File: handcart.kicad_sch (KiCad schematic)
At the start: 51 parts, among them J1 ROTARY ENCODER, J10 SPARE_SUPPLY, J12 SPARE_CHARGER, J13 SPARE_BMS, J14 ADD_FAN, J15 EXT_SCREEN, J16 CHARGER, J17 BMS, J2 ARROW_KEYS_1, J3 ARROW_KEYS_2, J4 ARROW_KEYS_3, J5 ARROW_KEYS_4, J6 RESET_BUTTON, J7 TSMS, J8 MUSHROOM, J9 1-776279-1, Q1 SSM3K361TU,LF, Q17 FQP17P06, U1 Tex_DCDC_v2, U2 DCDC2510

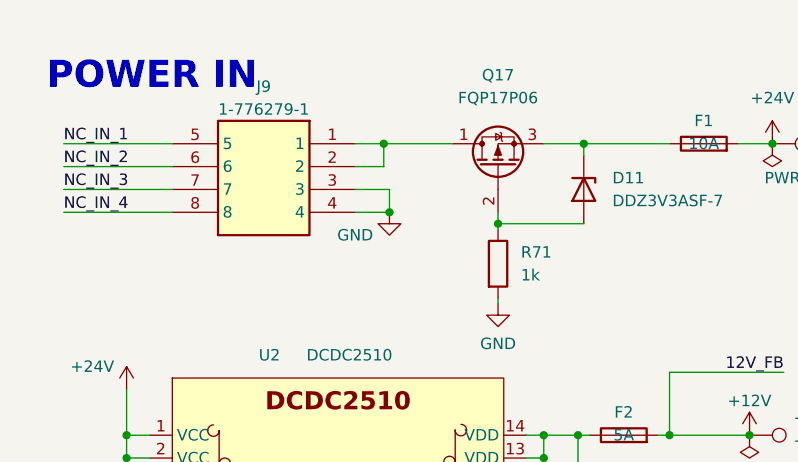
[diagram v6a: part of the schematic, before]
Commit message: Fixed vias diameter, fixed width of the input trace to the DCDC, completed the front silkscreen and added the back silkscreen
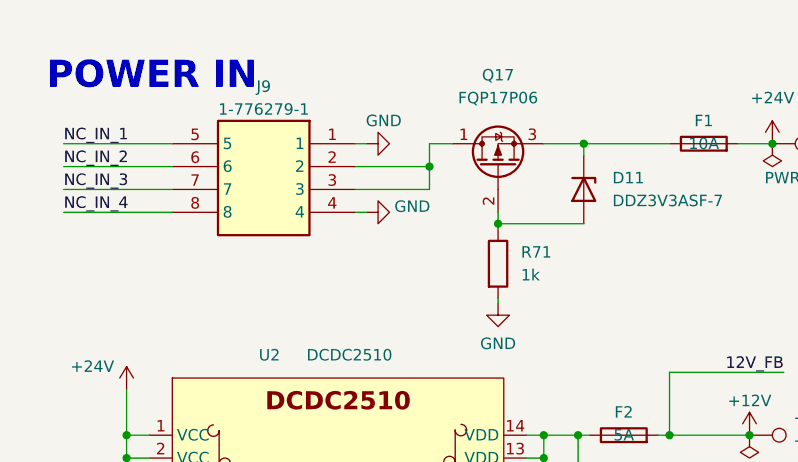
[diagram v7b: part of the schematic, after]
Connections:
- net GND: now also J9.1; no longer J9.3
- net at J9.2, Q17.1 (D): now also J9.3; no longer J9.1
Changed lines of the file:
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@@
   (junction (at 93.345 180.975) (diameter 0) (color 0 0 0 0)
   )
-  (junction (at 52.07 25.4) (diameter 0) (color 0 0 0 0)
-  )
   (junction (at 320.04 35.56) (diameter 0) (color 0 0 0 0)
   )
@@
   (junction (at 23.495 60.325) (diameter 0) (color 0 0 0 0)
   )
-  (junction (at 52.705 33.02) (diameter 0) (color 0 0 0 0)
-  )
   (junction (at 356.87 210.82) (diameter 0) (color 0 0 0 0)
   )
@@
   (junction (at 69.85 62.865) (diameter 0) (color 0 0 0 0)
   )
+  (junction (at 57.15 27.94) (diameter 0) (color 0 0 0 0)
+  )
   (junction (at 64.77 34.29) (diameter 0) (color 0 0 0 0)
   )
@@
   (no_connect (at 326.39 153.67))
   (no_connect (at 80.01 216.535))
-  (wire (pts (xy 52.07 25.4) (xy 59.69 25.4))
+  (wire (pts (xy 48.895 30.48) (xy 57.15 30.48))
     (stroke (width 0) (type default) (color 0 0 0 0))
   )
@@
     (stroke (width 0) (type default) (color 0 0 0 0))
   )
+  (wire (pts (xy 48.895 33.02) (xy 50.165 33.02))
+    (stroke (width 0) (type default) (color 0 0 0 0))
+  )
   (wire (pts (xy 346.71 229.87) (xy 349.25 229.87))
     (stroke (width 0) (type default) (color 0 0 0 0))
@@
     (stroke (width 0) (type default) (color 0 0 0 0))
   )
-  (wire (pts (xy 52.705 30.48) (xy 52.705 33.02))
-    (stroke (width 0) (type default) (color 0 0 0 0))
-  )
   (wire (pts (xy 49.53 133.35) (xy 49.53 134.62))
     (stroke (width 0) (type default) (color 0 0 0 0))
   )
-  (wire (pts (xy 48.895 27.94) (xy 52.07 27.94))
-    (stroke (width 0) (type default) (color 0 0 0 0))
-  )
   (wire (pts (xy 55.88 104.775) (xy 55.88 106.045))
     (stroke (width 0) (type default) (color 0 0 0 0))
@@
     (stroke (width 0) (type default) (color 0 0 0 0))
   )
-  (wire (pts (xy 48.895 30.48) (xy 52.705 30.48))
+  (wire (pts (xy 48.895 25.4) (xy 50.165 25.4))
     (stroke (width 0) (type default) (color 0 0 0 0))
   )
@@
     (stroke (width 0) (type default) (color 0 0 0 0))
   )
-  (wire (pts (xy 48.895 25.4) (xy 52.07 25.4))
-    (stroke (width 0) (type default) (color 0 0 0 0))
-  )
   (wire (pts (xy 44.45 201.295) (xy 53.34 201.295))
     (stroke (width 0) (type default) (color 0 0 0 0))
@@
     (stroke (width 0) (type default) (color 0 0 0 0))
   )
+  (wire (pts (xy 57.15 25.4) (xy 59.69 25.4))
+    (stroke (width 0) (type default) (color 0 0 0 0))
+  )
   (wire (pts (xy 66.04 99.695) (xy 71.12 99.695))
     (stroke (width 0) (type default) (color 0 0 0 0))
@@
     (stroke (width 0) (type default) (color 0 0 0 0))
   )
+  (wire (pts (xy 57.15 27.94) (xy 57.15 25.4))
+    (stroke (width 0) (type default) (color 0 0 0 0))
+  )
   (wire (pts (xy 72.39 146.685) (xy 80.645 146.685))
     (stroke (width 0) (type default) (color 0 0 0 0))
@@
     (stroke (width 0) (type default) (color 0 0 0 0))
   )
-  (wire (pts (xy 52.07 27.94) (xy 52.07 25.4))
-    (stroke (width 0) (type default) (color 0 0 0 0))
-  )
   (wire (pts (xy 132.715 121.92) (xy 156.21 121.92))
     (stroke (width 0) (type default) (color 0 0 0 0))
@@
     (stroke (width 0) (type default) (color 0 0 0 0))
   )
-  (wire (pts (xy 52.705 33.02) (xy 48.895 33.02))
-    (stroke (width 0) (type default) (color 0 0 0 0))
-  )
   (wire (pts (xy 314.325 101.6) (xy 348.615 101.6))
     (stroke (width 0) (type default) (color 0 0 0 0))
@@
     (stroke (width 0) (type default) (color 0 0 0 0))
   )
+  (wire (pts (xy 48.895 27.94) (xy 57.15 27.94))
+    (stroke (width 0) (type default) (color 0 0 0 0))
+  )
   (wire (pts (xy 90.17 216.535) (xy 93.345 216.535))
     (stroke (width 0) (type default) (color 0 0 0 0))
@@
     (stroke (width 0) (type default) (color 0 0 0 0))
   )
+  (wire (pts (xy 57.15 30.48) (xy 57.15 27.94))
+    (stroke (width 0) (type default) (color 0 0 0 0))
+  )
   (wire (pts (xy 205.74 144.78) (xy 205.74 151.13))
     (stroke (width 0) (type default) (color 0 0 0 0))
@@
     (pin "3")
   )
-  (symbol (lib_id "power:GND") (at 52.705 33.02 0) (mirror y) (unit 1)
+  (symbol (lib_id "power:GND") (at 50.165 25.4 90) (mirror x) (unit 1)
     (in_bom yes) (on_board yes)
-    (property "Reference" "#PWR014" (id 0) (at 52.705 39.37 0)
+    (property "Reference" "#PWR014" (id 0) (at 56.515 25.4 0)
       (effects (font (size 1.27 1.27)) hide)
     )
-    (property "Value" "GND" (id 1) (at 48.895 35.56 0))
-    (property "Footprint" "" (id 2) (at 52.705 33.02 0)
+    (property "Value" "GND" (id 1) (at 52.07 22.86 90))
+    (property "Footprint" "" (id 2) (at 50.165 25.4 0)
       (effects (font (size 1.27 1.27)) hide)
     )
-    (property "Datasheet" "" (id 3) (at 52.705 33.02 0)
+    (property "Datasheet" "" (id 3) (at 50.165 25.4 0)
       (effects (font (size 1.27 1.27)) hide)
     )
@@
     (pin "1")
   )
+  (symbol (lib_id "power:GND") (at 50.165 33.02 90) (mirror x) (unit 1)
+    (in_bom yes) (on_board yes)
+    (property "Reference" "#PWR0172" (id 0) (at 56.515 33.02 0)
+      (effects (font (size 1.27 1.27)) hide)
+    )
+    (property "Value" "GND" (id 1) (at 55.245 32.385 90))
+    (property "Footprint" "" (id 2) (at 50.165 33.02 0)
+      (effects (font (size 1.27 1.27)) hide)
+    )
+    (property "Datasheet" "" (id 3) (at 50.165 33.02 0)
+      (effects (font (size 1.27 1.27)) hide)
+    )
+    (pin "1")
+  )
   (symbol (lib_id "power:+5V") (at 309.245 91.44 0) (unit 1)
     (in_bom yes) (on_board yes)
@@
       (reference "#PWR0171") (unit 1) (value "GND") (footprint "")
     )
+    (path "/48ed129a-d652-4227-9455-06dfa73a7464"
+      (reference "#PWR0172") (unit 1) (value "GND") (footprint "")
+    )
     (path "/5423ac07-d0aa-443c-8aa6-dc2e9e5796c3/20a21468-72b8-4aa3-af31-6cfbf5c1d3f5"

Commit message: Fixed Schematic, fixed some traces. Still not finished
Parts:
- removed J10: SPARE_SUPPLY, Connector_Molex:Molex_Micro-Fit_3.0_43045-1012_2x05_P3.00mm_Vertical, symbol Connector_Generic:Conn_02x05_Odd_Even
- removed J12: SPARE_CHARGER, Connector_Molex:Molex_Micro-Fit_3.0_43045-0612_2x03_P3.00mm_Vertical, symbol Connector_Generic:Conn_02x03_Odd_Even
- added J10: SPARE_SUPPLY, Connector_Molex:Molex_Micro-Fit_3.0_43045-1012_2x05_P3.00mm_Vertical, symbol Connector_Generic:Conn_02x05_Top_Bottom
- added J12: SPARE_CHARGER, Connector_Molex:Molex_Micro-Fit_3.0_43045-0612_2x03_P3.00mm_Vertical, symbol Connector_Generic:Conn_02x03_Top_Bottom
- D1: footprint Diode_SMD:D_SOD-323_HandSoldering -> Diode_SMD:D_SOD-123
- J9: footprint Eagle_Connectors:17762791 -> Eagle_Connectors:TE-17762791
- JP1: value RASPBERRY_bypass -> RASPI_BYPASS
- Q17: symbol Device:Q_PMOS_DGS -> Device:Q_PMOS_GDS
- TP1: value TP_3V3 -> 3V3
- TP2: value TP_5V -> 5V
- TP3: value TP_24V -> 24V
- TP4: value TP_12V -> 12V
- TP5: value TP_VSD -> VSD
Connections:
- net +12V: now also J10.3 (Pin_3)
- net +24V: now also J10.1 (Pin_1)
- net +3V3: now also J10.4 (Pin_4)
- net +5V: now also J10.2 (Pin_2)
- net GND: now also J10.5 (Pin_5), J10.6 (Pin_6)
- net NC_CRG_1: now also J12.1 (Pin_1)
- net NC_CRG_2: now also J12.2 (Pin_2)
- net NC_CRG_3: now also J12.3 (Pin_3)
- net NC_CRG_4: now also J12.4 (Pin_4)
- net NC_CRG_5: now also J12.5 (Pin_5)
- net NC_CRG_6: now also J12.6 (Pin_6)
- net NC_IN_1: now also J10.7 (Pin_7)
- net NC_IN_2: now also J10.9 (Pin_9)
- net NC_IN_3: now also J10.8 (Pin_8)
- net NC_IN_4: now also J10.10 (Pin_10)
- net at D11.2 (A), R71.1: now also Q17.1 (G); no longer Q17.2 (G)
- net at J9.2, J9.3: now also Q17.2 (D); no longer Q17.1 (D)
- net VCC renamed VSD
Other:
- sheet Output renamed Indicators
- sheet Indicators: file Output.kicad_sch -> Indicators.kicad_sch
- sheet Indicators ports: added ADD_FAN_PWM, SCL, SDA, ~{OE}; removed RASPY_STRIP1_B, RASPY_STRIP1_G, RASPY_STRIP1_R, RASPY_TSAL_B, RASPY_TSAL_G, RASPY_TSAL_R
- sheet RS_232+FEEDBACK ports: added RELAY_SUTHDOWN_FB; removed COOLING_1, COOLING_2, RELE_SUTHDOWN_FB
- sheet Raspberry ports: added SCL, SDA, ~{OE}; removed ADD_FAN_PWM, RASPY_STRIP1_B, RASPY_STRIP1_G, RASPY_STRIP1_R, RASPY_TSAL_B, RASPY_TSAL_G, RASPY_TSAL_R
- sheet Shutdown+Discharge ports: added RELAY_SHUTDOWN_FB; removed RELE_SHUTDOWN_FB
- note added: "INDICATORS"
- note added: "RASPBERRY"
- note added: "RS232+FEEDBACK"
- note added: "SHUTDOWN+DISCHARGE"
